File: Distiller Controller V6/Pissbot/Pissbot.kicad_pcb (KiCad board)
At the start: 2 copper layers, 2 parts

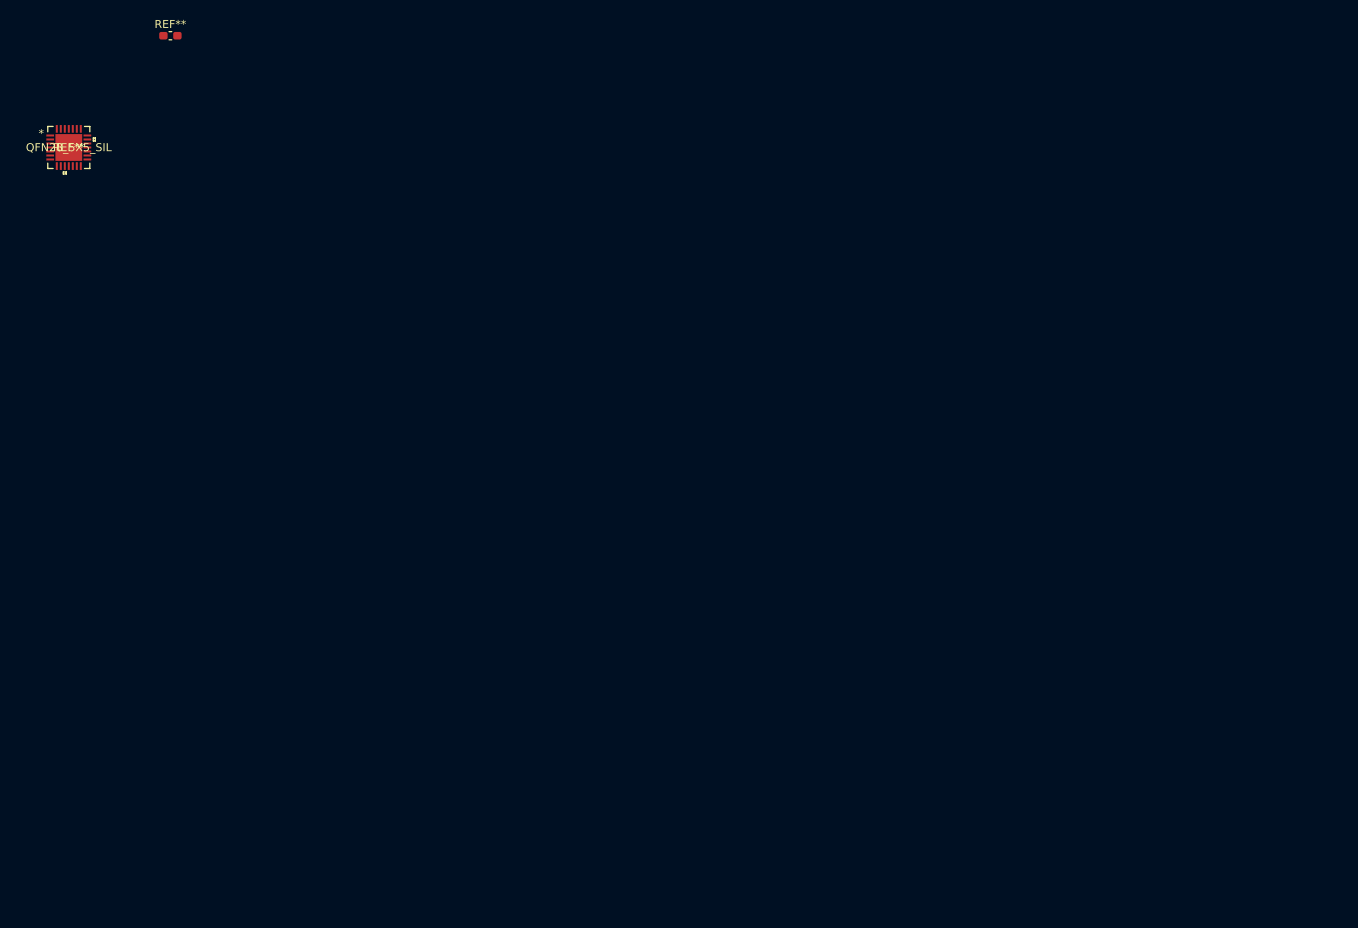
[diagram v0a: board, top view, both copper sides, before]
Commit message: Updated PCB. Added library files
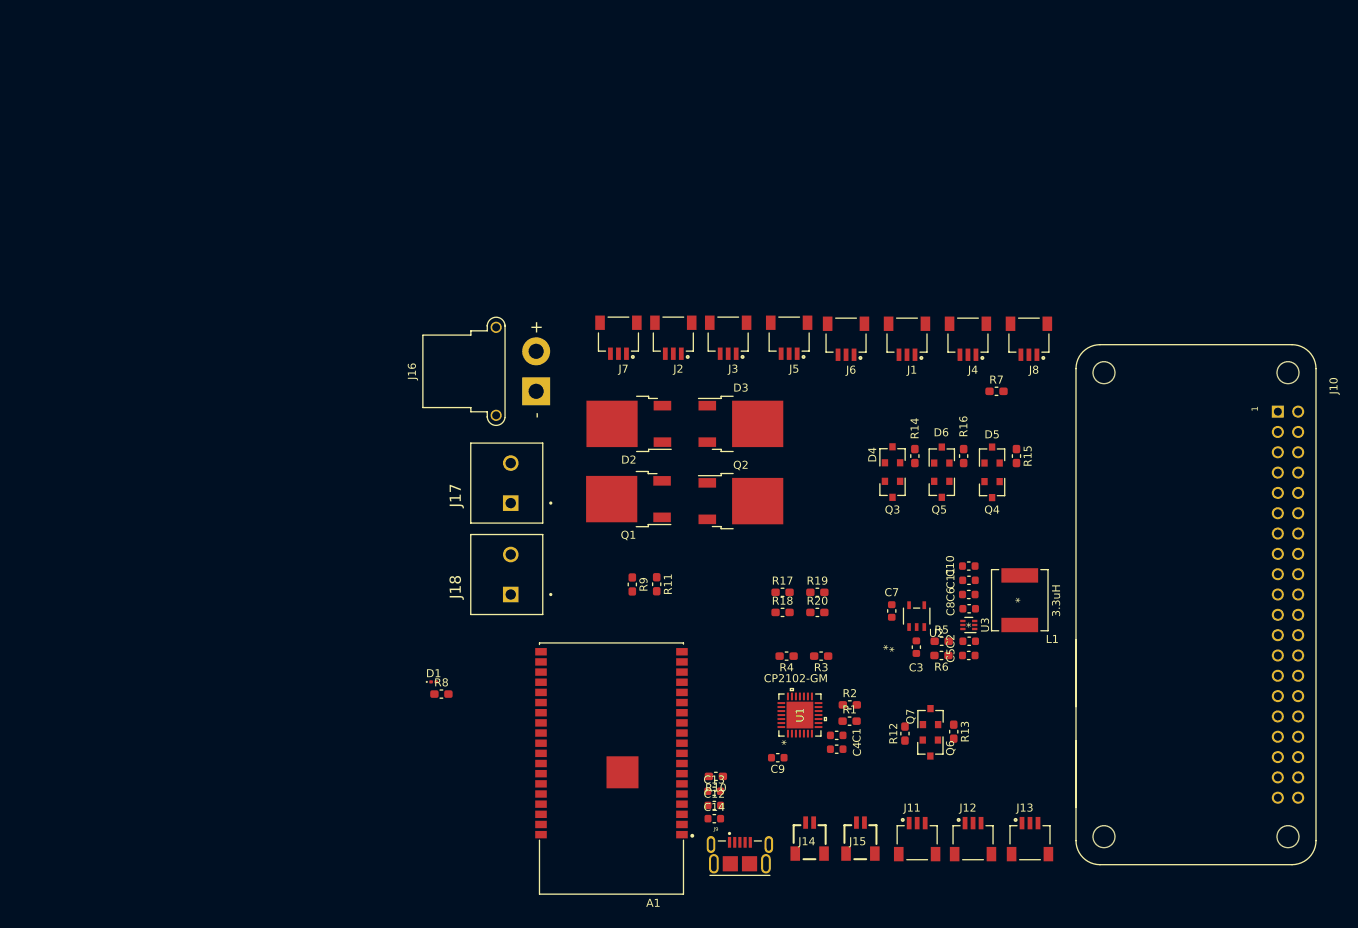
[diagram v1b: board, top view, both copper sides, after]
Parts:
- removed REF**: R_0603_1608Metric_Pad1.05x0.95mm_HandSolder, Resistor_SMD:R_0603_1608Metric_Pad1.05x0.95mm_HandSolder
- removed REF**: QFN28_5X5_SIL, footprints:CP2102-GM
- added A1: ESP32-WROVER-I, ESP32-WROVER-I:XCVR_ESP32-WROVER-I, F.Cu at (137.7, 127.2)
- added C1: 4.7uF, Capacitor_SMD:C_0603_1608Metric, F.Cu at (165.8, 123.0)
- added C10: 22uF, Capacitor_SMD:C_0603_1608Metric, F.Cu at (182.3, 101.9)
- added C11: 0.1uF, Capacitor_SMD:C_0603_1608Metric, F.Cu at (182.4, 103.6)
- added C12: 22uF, Capacitor_SMD:C_0603_1608Metric, F.Cu at (150.5, 131.8)
- added C13: 0.1uF, Capacitor_SMD:C_0603_1608Metric, F.Cu at (150.5, 130.0)
- added C14: 0.1uF, Capacitor_SMD:C_0603_1608Metric, F.Cu at (150.5, 133.4)
- added C2: 10uF, Capacitor_SMD:C_0603_1608Metric, F.Cu at (182.4, 111.3)
- added C3: 1uF, Capacitor_SMD:C_0603_1608Metric, F.Cu at (175.8, 112.0)
- added C4: 0.1uF, Capacitor_SMD:C_0603_1608Metric, F.Cu at (165.8, 124.7)
- added C5: 10uF, Capacitor_SMD:C_0603_1608Metric, F.Cu at (182.3, 113.0)
- added C6: 10uF, Capacitor_SMD:C_0603_1608Metric, F.Cu at (182.3, 105.4)
- added C7: 1uF, Capacitor_SMD:C_0603_1608Metric, F.Cu at (172.7, 107.5)
- added C8: 0.1uF, Capacitor_SMD:C_0603_1608Metric, F.Cu at (182.4, 107.2)
- added C9: 22uF, Capacitor_SMD:C_0603_1608Metric, F.Cu at (158.5, 125.8)
- added D1: LED_Small, LED_SMD:LED_0201_0603Metric, F.Cu at (115.5, 116.3)
- added D2: MBRD835TR, Package_TO_SOT_SMD:TO-252-2, F.Cu at (139.9, 84.1)
- added D3: MBRD835TR, Package_TO_SOT_SMD:TO-252-2, F.Cu at (153.9, 84.1)
- added D4: 9.1V, Package_TO_SOT_SMD:SOT-23, F.Cu at (172.8, 87.9)
- added D5: 9.1V, Package_TO_SOT_SMD:SOT-23, F.Cu at (185.3, 88.0)
- added D6: 9.1V, Package_TO_SOT_SMD:SOT-23, F.Cu at (179.0, 88.0)
- added J1: T1, JST-SH 3 Connector:JST_SM03B-SRSS-TB(LF)(SN), F.Cu at (174.6, 75.4)
- added J10: Raspberry_Pi_2_3, PiZero:ADA3708_RPI-ZERO, F.Cu at (222.2, 106.7)
- added J11: T4, JST-SH 3 Connector:JST_SM03B-SRSS-TB(LF)(SN), F.Cu at (175.9, 134.0)
- added J12: T4, JST-SH 3 Connector:JST_SM03B-SRSS-TB(LF)(SN), F.Cu at (182.9, 134.0)
- added J13: T4, JST-SH 3 Connector:JST_SM03B-SRSS-TB(LF)(SN), F.Cu at (190.0, 134.0)
- added J14: SM02B-SRSS-TB(LF)(SN), JST SH 2Pin:SM02B-SRSS-TB(LF)(SN), F.Cu at (162.5, 135.9)
- added J15: SM02B-SRSS-TB(LF)(SN), JST SH 2Pin:SM02B-SRSS-TB(LF)(SN), F.Cu at (168.8, 135.9)
- added J16: Conn_01x02_Female, Connector_AMASS:AMASS_XT30PW-F_1x02_P2.50mm_Horizontal, F.Cu at (128.3, 80.0)
- added J17: Conn_01x02_Female, Screw Terminal - TB001:CUI_TB001-500-02BE, F.Cu at (125.1, 94.0)
- added J18: Conn_01x02_Female, Screw Terminal - TB001:CUI_TB001-500-02BE, F.Cu at (125.1, 105.4)
- added J2: T5, JST-SH 3 Connector:JST_SM03B-SRSS-TB(LF)(SN), F.Cu at (145.4, 75.3)
- added J3: T2, JST-SH 3 Connector:JST_SM03B-SRSS-TB(LF)(SN), F.Cu at (152.3, 75.3)
- added J4: T6, JST-SH 3 Connector:JST_SM03B-SRSS-TB(LF)(SN), F.Cu at (182.2, 75.4)
- added J5: T3, JST-SH 3 Connector:JST_SM03B-SRSS-TB(LF)(SN), F.Cu at (159.9, 75.3)
- added J6: T7, JST-SH 3 Connector:JST_SM03B-SRSS-TB(LF)(SN), F.Cu at (167.0, 75.4)
- added J7: T4, JST-SH 3 Connector:JST_SM03B-SRSS-TB(LF)(SN), F.Cu at (138.6, 75.3)
- added J8: T8, JST-SH 3 Connector:JST_SM03B-SRSS-TB(LF)(SN), F.Cu at (189.9, 75.4)
- added J9: MicroUSB_ESP, Micro USB:Micro-USB-TE_2040002-1, F.Cu at (153.7, 139.1)
- added L1: 3.3uH, 3_3uH_ECSMPIL06303R3MC:ECS-MPIL0630-3R3MC, F.Cu at (188.7, 106.1)
- added Q1: MCU80N03A-TP, Package_TO_SOT_SMD:TO-252-2, F.Cu at (139.8, 93.5)
- added Q2: MCU80N03A-TP, Package_TO_SOT_SMD:TO-252-2, F.Cu at (153.9, 93.7)
- added Q3: SSM3J338R, Package_TO_SOT_SMD:SOT-23, F.Cu at (172.8, 92.3)
- added Q4: SSM3J338R, Package_TO_SOT_SMD:SOT-23, F.Cu at (185.3, 92.3)
- added Q5: SSM3J338R, Package_TO_SOT_SMD:SOT-23, F.Cu at (179.0, 92.3)
- added Q6: S8050, Package_TO_SOT_SMD:SOT-23, F.Cu at (177.5, 124.6)
- added Q7: S8050, Package_TO_SOT_SMD:SOT-23, F.Cu at (177.6, 120.7)
- added R1: 22.1k, Resistor_SMD:R_0603_1608Metric_Pad1.05x0.95mm_HandSolder, F.Cu at (167.4, 121.2)
- added R10: 10k, Resistor_SMD:R_0603_1608Metric_Pad1.05x0.95mm_HandSolder, F.Cu at (150.7, 128.1)
- added R11: 4.7k, Resistor_SMD:R_0603_1608Metric_Pad1.05x0.95mm_HandSolder, F.Cu at (143.3, 104.1)
- added R12: 10k, Resistor_SMD:R_0603_1608Metric_Pad1.05x0.95mm_HandSolder, F.Cu at (174.4, 122.8)
- added R13: 10k, Resistor_SMD:R_0603_1608Metric_Pad1.05x0.95mm_HandSolder, F.Cu at (180.5, 122.6)
- added R14: 100k, Resistor_SMD:R_0603_1608Metric_Pad1.05x0.95mm_HandSolder, F.Cu at (175.6, 88.1)
- added R15: 100k, Resistor_SMD:R_0603_1608Metric_Pad1.05x0.95mm_HandSolder, F.Cu at (188.3, 88.1)
- added R16: 100k, Resistor_SMD:R_0603_1608Metric_Pad1.05x0.95mm_HandSolder, F.Cu at (181.7, 88.1)
- added R17: 2k, Resistor_SMD:R_0603_1608Metric_Pad1.05x0.95mm_HandSolder, F.Cu at (159.1, 105.1)
- added R18: 2k, Resistor_SMD:R_0603_1608Metric_Pad1.05x0.95mm_HandSolder, F.Cu at (159.1, 107.6)
- added R19: 2k, Resistor_SMD:R_0603_1608Metric_Pad1.05x0.95mm_HandSolder, F.Cu at (163.4, 105.1)
- added R2: 47.5k, Resistor_SMD:R_0603_1608Metric_Pad1.05x0.95mm_HandSolder, F.Cu at (167.5, 119.2)
- added R20: 2k, Resistor_SMD:R_0603_1608Metric_Pad1.05x0.95mm_HandSolder, F.Cu at (163.4, 107.6)
- added R3: 2k, Resistor_SMD:R_0603_1608Metric_Pad1.05x0.95mm_HandSolder, F.Cu at (163.9, 113.1)
- added R4: 10k, Resistor_SMD:R_0603_1608Metric_Pad1.05x0.95mm_HandSolder, F.Cu at (159.6, 113.1)
- added R5: 73.2k, Resistor_SMD:R_0603_1608Metric_Pad1.05x0.95mm_HandSolder, F.Cu at (179.0, 111.3)
- added R6: 10k, Resistor_SMD:R_0603_1608Metric_Pad1.05x0.95mm_HandSolder, F.Cu at (178.9, 113.0)
- added R7: 2k, Resistor_SMD:R_0603_1608Metric_Pad1.05x0.95mm_HandSolder, F.Cu at (185.8, 80.0)
- added R8: 1k, Resistor_SMD:R_0603_1608Metric_Pad1.05x0.95mm_HandSolder, F.Cu at (116.4, 117.9)
- added R9: 4.7k, Resistor_SMD:R_0603_1608Metric_Pad1.05x0.95mm_HandSolder, F.Cu at (140.3, 104.2)
- added U1: CP2102-GM, footprints:CP2102-GM, F.Cu at (161.2, 120.5)
- added U2: TLV74033PDBVR, TLV74033PDBVR:TLV74033PDBVR, F.Cu at (175.8, 108.1)
- added U3: TPS563231DRLR, TPS563231DRLR:TPS563231DRLR, F.Cu at (182.4, 109.2)
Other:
- copper layers 2 -> 4
